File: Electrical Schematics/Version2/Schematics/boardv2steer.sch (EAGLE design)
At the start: 19 parts, among them IC3 VNH2SP30-E, J2 PHOENIX_2POS_1792863, Q1 IRFR3707Z, Q2 IRFR3707Z

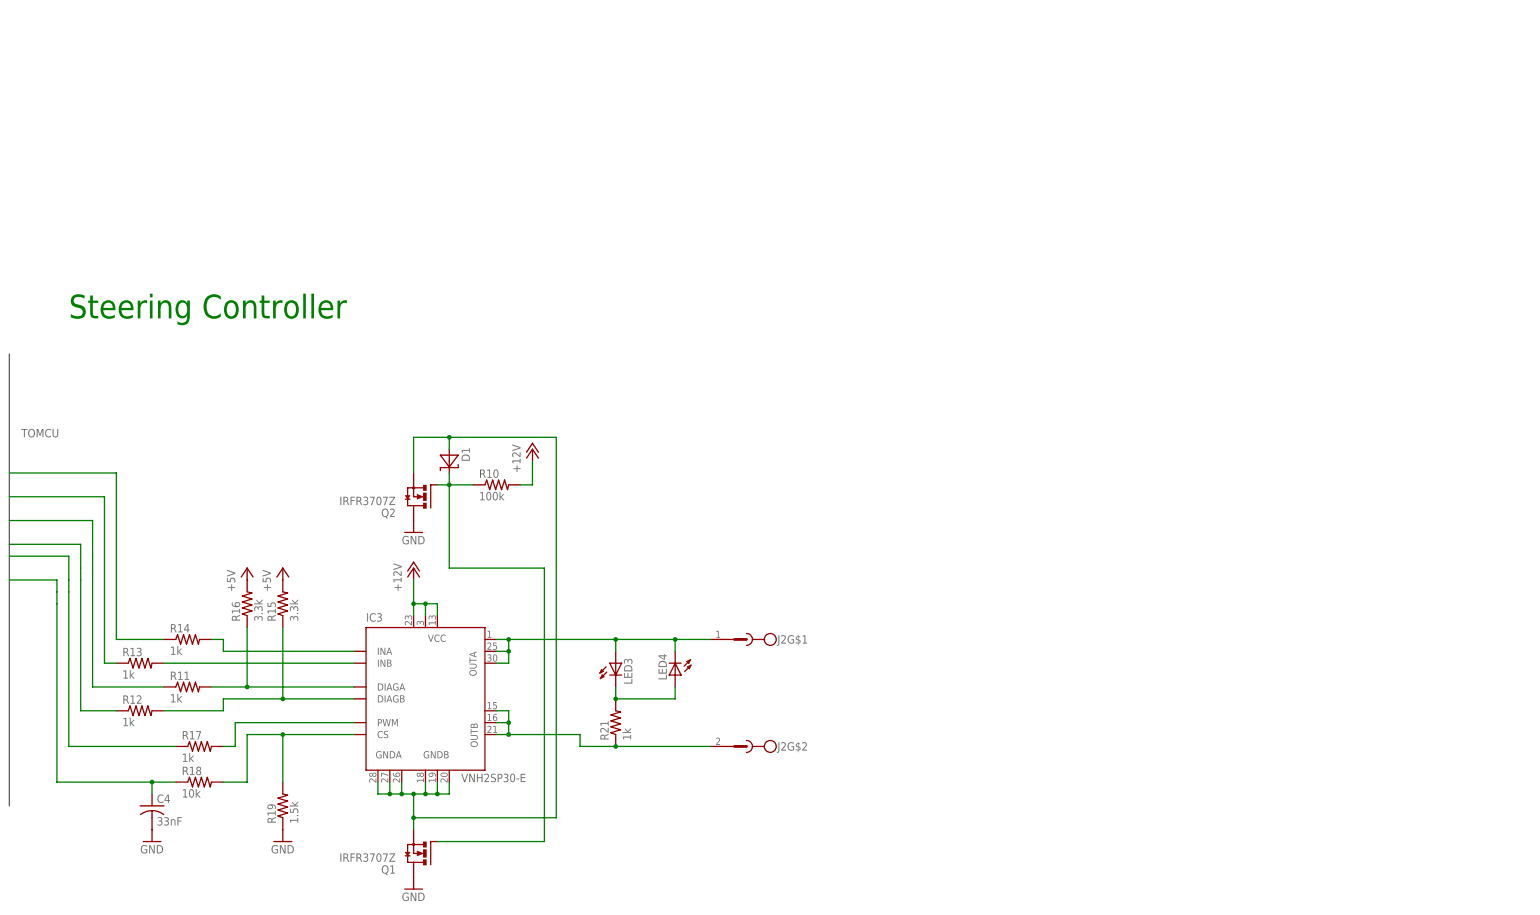
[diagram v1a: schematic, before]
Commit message: commiting justins changes to the steering controller
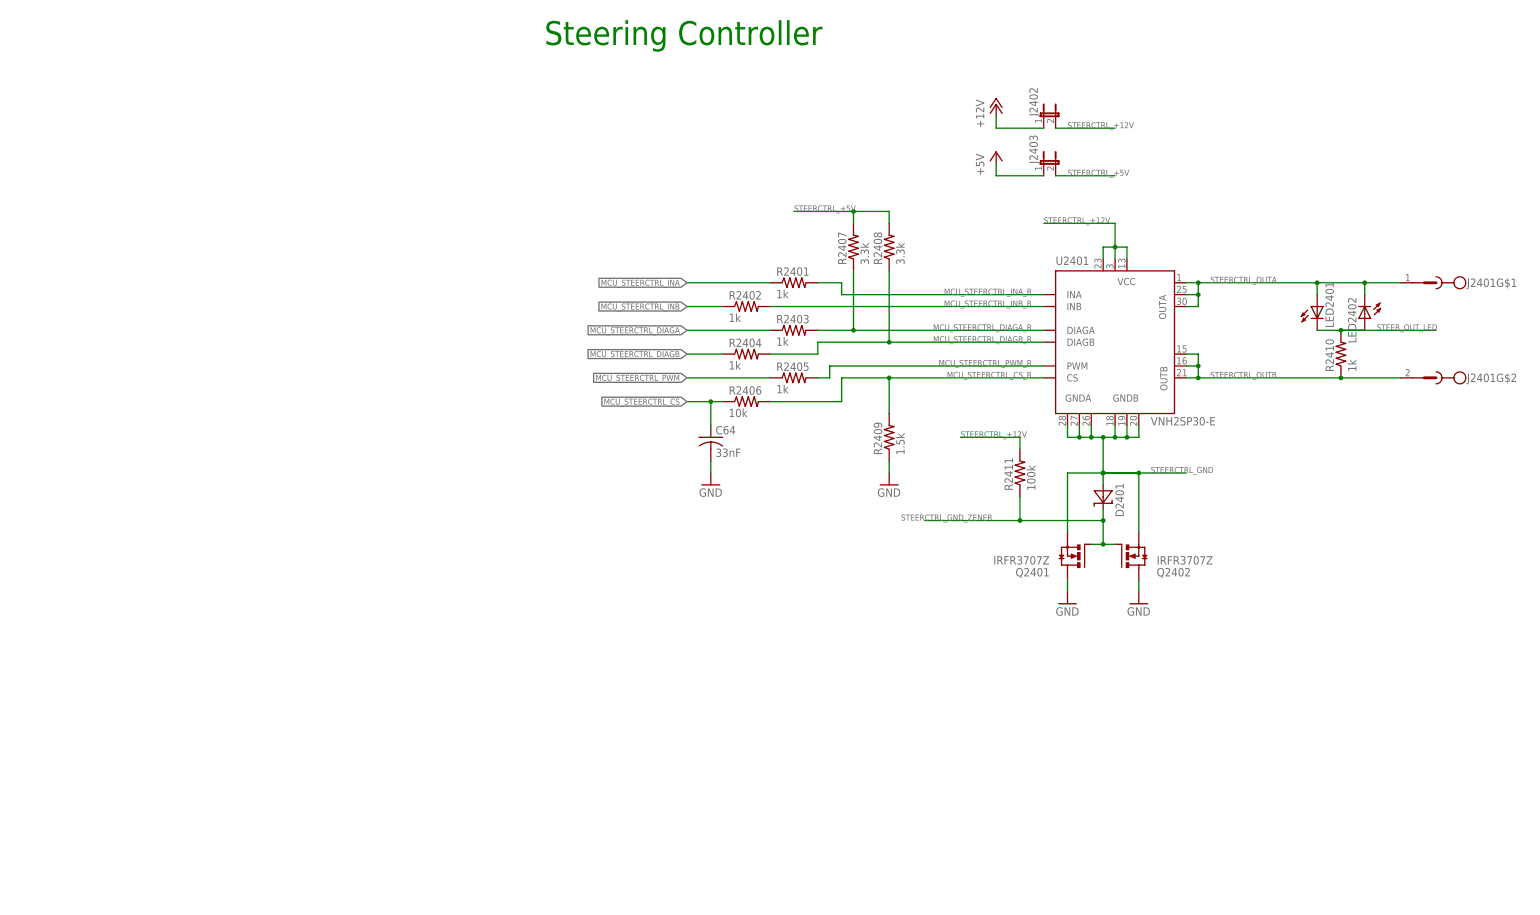
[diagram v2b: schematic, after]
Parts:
- removed C4: 33nF, rcl:C-USC1206K
- removed D1: ZENER_SOD123, Atlanta Robotics:ZENER_SOD123
- removed IC3: VNH2SP30-E, st-microelectronics:VNH2SP30-E
- removed J2: PHOENIX_2POS_1792863, Atlanta-Robotics LAPTOP:PHOENIX_2POS_1792863
- removed LED3, LED4: (no value), led:LEDSML1206
- removed Q1, Q2: IRFR3707Z, Atlanta Robotics:IRFR3707Z
- removed R10: 100k, rcl:R-US_R1206W
- removed R11, R12, R13, R14, R17, R21: 1k, rcl:R-US_R1206W
- removed R15, R16: 3.3k, rcl:R-US_R1206W
- removed R18: 10k, rcl:R-US_R1206W
- removed R19: 1.5k, rcl:R-US_R1206W
- added C64: 33nF, rcl:C-USC1206K
- added D2401: ZENER_SOD123, Atlanta Robotics:ZENER_SOD123
- added J2401: PHOENIX_2POS_1792863, Atlanta-Robotics LAPTOP:PHOENIX_2POS_1792863
- added J2402, J2403: (no value), jumper:JP1E
- added LED2401, LED2402: (no value), led:LEDSML1206
- added Q2401, Q2402: IRFR3707Z, Atlanta Robotics:IRFR3707Z
- added R2401, R2402, R2403, R2404, R2405, R2410: 1k, rcl:R-US_R1206W
- added R2406: 10k, rcl:R-US_R1206W
- added R2407, R2408: 3.3k, rcl:R-US_R1206W
- added R2409: 1.5k, rcl:R-US_R1206W
- added R2411: 100k, rcl:R-US_R1206W
- added U2401: VNH2SP30-E, st-microelectronics:VNH2SP30-E
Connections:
- removed net B$1: C4.1, R11.1, R12.1, R13.1, R14.1, R17.1, R18.1
- removed net N$10: D1.A, IC3.GNDA, IC3.GNDA@1, IC3.GNDA@2, IC3.GNDB, IC3.GNDB@1, IC3.GNDB@2, Q1.S, Q2.S
- removed net N$17: IC3.INA, R14.2
- removed net N$18: IC3.INB, R13.2
- removed net N$19: IC3.DIAGA, R11.2, R16.1
- removed net N$20: IC3.DIAGB, R12.2, R15.1
- removed net N$21: IC3.PWM, R17.2
- removed net N$22: IC3.CS, R18.2, R19.2
- removed net N$24: IC3.OUTA, IC3.OUTA@1, IC3.OUTA@2, J2G$1.SK, LED3.A, LED4.C
- removed net N$25: IC3.OUTB, IC3.OUTB@1, IC3.OUTB@2, J2G$2.SK, R21.1
- removed net N$27: D1.C, Q1.G, Q2.G, R10.1
- removed net N$28: LED3.C, LED4.A, R21.2
- new net MCU_STEERCTRL_CS: C64.1, R2406.1
- new net MCU_STEERCTRL_CS_R: R2406.2, R2409.2, U2401.CS
- new net MCU_STEERCTRL_DIAGA: R2403.1
- new net MCU_STEERCTRL_DIAGA_R: R2403.2, R2407.1, U2401.DIAGA
- new net MCU_STEERCTRL_DIAGB: R2404.1
- new net MCU_STEERCTRL_DIAGB_R: R2404.2, R2408.1, U2401.DIAGB
- new net MCU_STEERCTRL_INA: R2401.1
- new net MCU_STEERCTRL_INA_R: R2401.2, U2401.INA
- new net MCU_STEERCTRL_INB: R2402.1
- new net MCU_STEERCTRL_INB_R: R2402.2, U2401.INB
- new net MCU_STEERCTRL_PWM: R2405.1
- new net MCU_STEERCTRL_PWM_R: R2405.2, U2401.PWM
- new net STEERCTRL_+12V: J2402.2, R2411.2, U2401.VCC, U2401.VCC@1, U2401.VCC@2
- new net STEERCTRL_+5V: J2403.2, R2407.2, R2408.2
- new net STEERCTRL_GND: D2401.A, Q2401.S, Q2402.S, U2401.GNDA, U2401.GNDA@1, U2401.GNDA@2, U2401.GNDB, U2401.GNDB@1, U2401.GNDB@2
- new net STEERCTRL_GND_ZENER: D2401.C, Q2401.G, Q2402.G, R2411.1
- new net STEERCTRL_OUTA: J2401G$1.SK, LED2401.A, LED2402.C, U2401.OUTA, U2401.OUTA@1, U2401.OUTA@2
- new net STEERCTRL_OUTB: J2401G$2.SK, R2410.1, U2401.OUTB, U2401.OUTB@1, U2401.OUTB@2
- new net STEER_OUT_LED: LED2401.C, LED2402.A, R2410.2
- net +12V: now also J2402.1; no longer IC3.VCC, IC3.VCC@1, IC3.VCC@2, R10.2
- net +5V: now also J2403.1; no longer R15.2, R16.2
- net GND: now also C64.2, Q2401.D, Q2402.D, R2409.1; no longer C4.2, Q1.D, Q2.D, R19.1

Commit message: updated circuits
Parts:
- removed D2401: ZENER_SOD123, Atlanta Robotics:ZENER_SOD123
- removed Q2401, Q2402: IRFR3707Z, Atlanta Robotics:IRFR3707Z
- removed R2411: 100k, rcl:R-US_R1206W
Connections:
- removed net STEERCTRL_GND: D2401.A, Q2401.S, Q2402.S, U2401.GNDA, U2401.GNDA@1, U2401.GNDA@2, U2401.GNDB, U2401.GNDB@1, U2401.GNDB@2
- removed net STEERCTRL_GND_ZENER: D2401.C, Q2401.G, Q2402.G, R2411.1
- net GND: now also U2401.GNDA, U2401.GNDA@1, U2401.GNDA@2, U2401.GNDB, U2401.GNDB@1, U2401.GNDB@2; no longer Q2401.D, Q2402.D
- net STEERCTRL_+12V: no longer R2411.2
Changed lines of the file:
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@@
 </classes>
 <parts>
-<part name="Q2402" library="Atlanta Robotics" deviceset="IRFR3707Z" device=""/>
-<part name="R2411" library="rcl" deviceset="R-US_" device="R1206W" value="100k"/>
-<part name="GND7" library="supply1" deviceset="GND" device=""/>
-<part name="D2401" library="Atlanta Robotics" deviceset="ZENER_SOD123" device=""/>
 <part name="R2403" library="rcl" deviceset="R-US_" device="R1206W" value="1k"/>
 <part name="R2404" library="rcl" deviceset="R-US_" device="R1206W" value="1k"/>
@@
 <part name="GND11" library="supply1" deviceset="GND" device=""/>
 <part name="P+8" library="supply1" deviceset="+5V" device=""/>
-<part name="Q2401" library="Atlanta Robotics" deviceset="IRFR3707Z" device=""/>
-<part name="GND16" library="supply1" deviceset="GND" device=""/>
 <part name="P+7" library="supply1" deviceset="+12V" device=""/>
 <part name="LED2401" library="led" deviceset="LED" device="SML1206"/>
@@
 <part name="J2402" library="jumper" deviceset="JP1E" device=""/>
 <part name="J2403" library="jumper" deviceset="JP1E" device=""/>
+<part name="SUPPLY1" library="supply2" deviceset="GND" device=""/>
 </parts>
 <sheets>
@@
 </plain>
 <instances>
-<instance part="Q2402" gate="G$1" x="152.4" y="63.5" rot="MR180"/>
-<instance part="R2411" gate="G$1" x="127" y="81.28" rot="R90"/>
-<instance part="GND7" gate="1" x="152.4" y="53.34"/>
-<instance part="D2401" gate="G$1" x="144.78" y="76.2" smashed="yes" rot="R270">
-<attribute name="NAME" x="147.4216" y="79.1464" size="1.778" layer="95" rot="R270"/>
-</instance>
 <instance part="R2403" gate="G$1" x="78.74" y="111.76"/>
 <instance part="R2404" gate="G$1" x="68.58" y="106.68"/>
@@
 <instance part="GND11" gate="1" x="99.06" y="78.74"/>
 <instance part="P+8" gate="1" x="121.92" y="149.86"/>
-<instance part="Q2401" gate="G$1" x="137.16" y="63.5" rot="R180"/>
-<instance part="GND16" gate="1" x="137.16" y="53.34"/>
 <instance part="P+7" gate="1" x="121.92" y="160.02"/>
 <instance part="LED2401" gate="G$1" x="190.5" y="116.84"/>
@@
 <instance part="J2402" gate="A" x="132.08" y="157.48"/>
 <instance part="J2403" gate="A" x="132.08" y="147.32"/>
+<instance part="SUPPLY1" gate="GND" x="144.78" y="73.66"/>
 </instances>
 <busses>
@@
 <net name="GND" class="0">
 <segment>
-<pinref part="Q2402" gate="G$1" pin="D"/>
-<pinref part="GND7" gate="1" pin="GND"/>
-<wire x1="152.4" y1="55.88" x2="152.4" y2="58.42" width="0.1524" layer="91"/>
-</segment>
-<segment>
 <pinref part="C64" gate="G$1" pin="2"/>
 <pinref part="GND10" gate="1" pin="GND"/>
@@
 </segment>
 <segment>
-<pinref part="Q2401" gate="G$1" pin="D"/>
-<pinref part="GND16" gate="1" pin="GND"/>
-<wire x1="137.16" y1="55.88" x2="137.16" y2="58.42" width="0.1524" layer="91"/>
-</segment>
-</net>
-<net name="STEERCTRL_GND" class="0">
-<segment>
-<pinref part="U2401" gate="G$1" pin="GNDA@2"/>
-<wire x1="137.16" y1="91.44" x2="137.16" y2="88.9" width="0.1524" layer="91"/>
 <pinref part="U2401" gate="G$1" pin="GNDB@2"/>
-<wire x1="137.16" y1="88.9" x2="139.7" y2="88.9" width="0.1524" layer="91"/>
-<wire x1="139.7" y1="88.9" x2="142.24" y2="88.9" width="0.1524" layer="91"/>
-<wire x1="142.24" y1="88.9" x2="144.78" y2="88.9" width="0.1524" layer="91"/>
-<wire x1="144.78" y1="88.9" x2="147.32" y2="88.9" width="0.1524" layer="91"/>
-<wire x1="147.32" y1="88.9" x2="149.86" y2="88.9" width="0.1524" layer="91"/>
+<wire x1="152.4" y1="88.9" x2="152.4" y2="91.44" width="0.1524" layer="91"/>
 <wire x1="149.86" y1="88.9" x2="152.4" y2="88.9" width="0.1524" layer="91"/>
-<wire x1="152.4" y1="88.9" x2="152.4" y2="91.44" width="0.1524" layer="91"/>
 <pinref part="U2401" gate="G$1" pin="GNDB@1"/>
 <wire x1="149.86" y1="91.44" x2="149.86" y2="88.9" width="0.1524" layer="91"/>
 <junction x="149.86" y="88.9"/>
+<wire x1="147.32" y1="88.9" x2="149.86" y2="88.9" width="0.1524" layer="91"/>
 <pinref part="U2401" gate="G$1" pin="GNDB"/>
 <wire x1="147.32" y1="91.44" x2="147.32" y2="88.9" width="0.1524" layer="91"/>
 <junction x="147.32" y="88.9"/>
+<wire x1="142.24" y1="88.9" x2="144.78" y2="88.9" width="0.1524" layer="91"/>
 <pinref part="U2401" gate="G$1" pin="GNDA"/>
+<wire x1="144.78" y1="88.9" x2="147.32" y2="88.9" width="0.1524" layer="91"/>
 <wire x1="142.24" y1="91.44" x2="142.24" y2="88.9" width="0.1524" layer="91"/>
 <junction x="142.24" y="88.9"/>
+<wire x1="139.7" y1="88.9" x2="142.24" y2="88.9" width="0.1524" layer="91"/>
 <pinref part="U2401" gate="G$1" pin="GNDA@1"/>
 <wire x1="139.7" y1="91.44" x2="139.7" y2="88.9" width="0.1524" layer="91"/>
 <junction x="139.7" y="88.9"/>
+<pinref part="U2401" gate="G$1" pin="GNDA@2"/>
+<wire x1="137.16" y1="91.44" x2="137.16" y2="88.9" width="0.1524" layer="91"/>
+<wire x1="137.16" y1="88.9" x2="139.7" y2="88.9" width="0.1524" layer="91"/>
+<wire x1="144.78" y1="88.9" x2="144.78" y2="76.2" width="0.1524" layer="91"/>
 <junction x="144.78" y="88.9"/>
-<wire x1="144.78" y1="88.9" x2="144.78" y2="81.28" width="0.1524" layer="91"/>
-<junction x="144.78" y="81.28"/>
-<pinref part="D2401" gate="G$1" pin="A"/>
-<wire x1="144.78" y1="81.28" x2="144.78" y2="78.74" width="0.1524" layer="91"/>
-<wire x1="144.78" y1="81.28" x2="152.4" y2="81.28" width="0.1524" layer="91"/>
-<junction x="144.78" y="81.28"/>
-<pinref part="Q2402" gate="G$1" pin="S"/>
-<wire x1="152.4" y1="81.28" x2="152.4" y2="68.58" width="0.1524" layer="91"/>
-<label x="154.94" y="81.28" size="1.27" layer="95"/>
-<pinref part="Q2401" gate="G$1" pin="S"/>
-<wire x1="137.16" y1="68.58" x2="137.16" y2="81.28" width="0.1524" layer="91"/>
-<wire x1="137.16" y1="81.28" x2="144.78" y2="81.28" width="0.1524" layer="91"/>
-<wire x1="144.78" y1="81.28" x2="152.4" y2="81.28" width="0.1524" layer="91"/>
-<junction x="152.4" y="81.28"/>
-<wire x1="152.4" y1="81.28" x2="162.56" y2="81.28" width="0.1524" layer="91"/>
+<pinref part="SUPPLY1" gate="GND" pin="GND"/>
+<junction x="144.78" y="76.2"/>
 </segment>
 </net>
@@
 <pinref part="J2401" gate="G$2" pin="SK"/>
 <label x="167.64" y="101.6" size="1.27" layer="95"/>
+<junction x="165.1" y="106.68"/>
 </segment>
 </net>
@@
 <junction x="60.96" y="96.52"/>
 <label x="55.88" y="96.52" size="1.27" layer="95" rot="R180" xref="yes"/>
-</segment>
-</net>
-<net name="STEERCTRL_GND_ZENER" class="0">
-<segment>
-<pinref part="R2411" gate="G$1" pin="1"/>
-<wire x1="127" y1="76.2" x2="127" y2="71.12" width="0.1524" layer="91"/>
-<wire x1="127" y1="71.12" x2="144.78" y2="71.12" width="0.1524" layer="91"/>
-<label x="101.6" y="71.12" size="1.27" layer="95"/>
-<wire x1="127" y1="71.12" x2="106.68" y2="71.12" width="0.1524" layer="91"/>
-<pinref part="D2401" gate="G$1" pin="C"/>
-<wire x1="144.78" y1="73.66" x2="144.78" y2="71.12" width="0.1524" layer="91"/>
-<pinref part="Q2401" gate="G$1" pin="G"/>
-<pinref part="Q2402" gate="G$1" pin="G"/>
-<wire x1="142.24" y1="66.04" x2="144.78" y2="66.04" width="0.1524" layer="91"/>
-<wire x1="144.78" y1="66.04" x2="147.32" y2="66.04" width="0.1524" layer="91"/>
-<wire x1="144.78" y1="71.12" x2="144.78" y2="66.04" width="0.1524" layer="91"/>
-<junction x="144.78" y="71.12"/>
-<junction x="144.78" y="66.04"/>
-<junction x="127" y="71.12"/>
 </segment>
 </net>
@@
 </segment>
 <segment>
-<pinref part="R2411" gate="G$1" pin="2"/>
-<wire x1="127" y1="86.36" x2="127" y2="88.9" width="0.1524" layer="91"/>
-<wire x1="127" y1="88.9" x2="114.3" y2="88.9" width="0.1524" layer="91"/>
-<label x="114.3" y="88.9" size="1.27" layer="95"/>
-</segment>
-<segment>
